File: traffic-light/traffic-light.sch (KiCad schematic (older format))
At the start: 23 parts, among them J1 BATTERY, J10 Traffic_Light_4, J11 ICSP, J2 RFID-RC522_1, J3 RFID-RC522_2, J4 RFID-RC522_3, J5 RFID-RC522_4, J6 Ground, J7 Traffic_Light_1, J8 Traffic_Light_2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

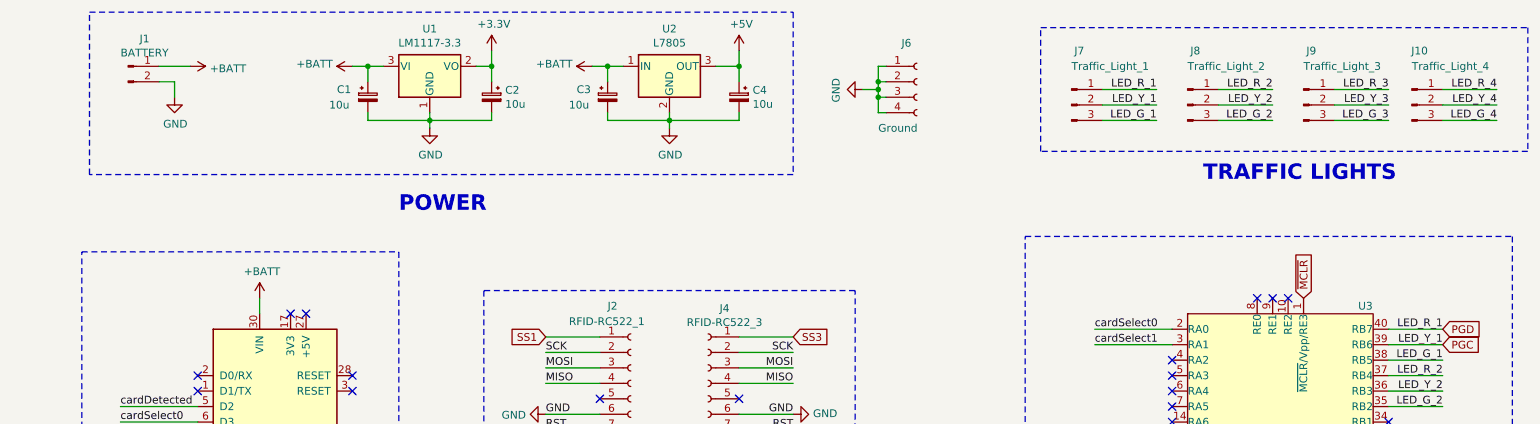
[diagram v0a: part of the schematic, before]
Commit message: Added diode and switch.
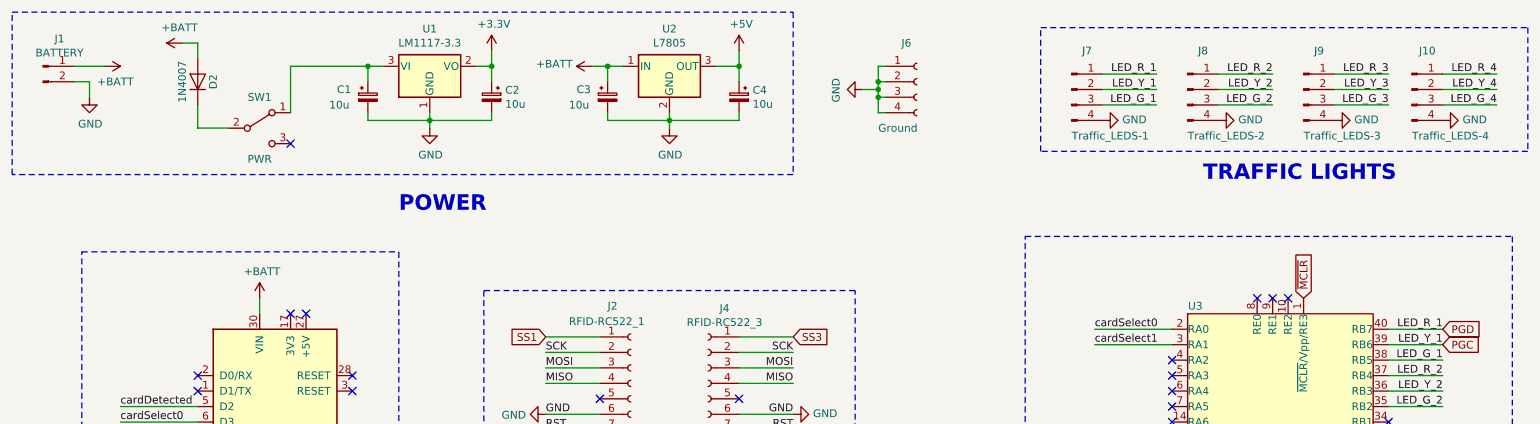
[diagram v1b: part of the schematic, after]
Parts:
- removed J10: Traffic_Light_4, Connector_PinHeader_2.54mm:PinHeader_1x03_P2.54mm_Vertical, symbol Connector:Conn_01x03_Male
- removed J7: Traffic_Light_1, Connector_PinHeader_2.54mm:PinHeader_1x03_P2.54mm_Vertical, symbol Connector:Conn_01x03_Male
- removed J8: Traffic_Light_2, Connector_PinHeader_2.54mm:PinHeader_1x03_P2.54mm_Vertical, symbol Connector:Conn_01x03_Male
- removed J9: Traffic_Light_3, Connector_PinHeader_2.54mm:PinHeader_1x03_P2.54mm_Vertical, symbol Connector:Conn_01x03_Male
- added D2: 1N4007, Diode_THT:D_DO-41_SOD81_P10.16mm_Horizontal, symbol Diode:1N4007
- added J10: Traffic_LEDS-4, Connector_PinHeader_2.54mm:PinHeader_1x04_P2.54mm_Vertical, symbol Connector:Conn_01x04_Male
- added J7: Traffic_LEDS-1, Connector_PinHeader_2.54mm:PinHeader_1x04_P2.54mm_Vertical, symbol Connector:Conn_01x04_Male
- added J8: Traffic_LEDS-2, Connector_PinHeader_2.54mm:PinHeader_1x04_P2.54mm_Vertical, symbol Connector:Conn_01x04_Male
- added J9: Traffic_LEDS-3, Connector_PinHeader_2.54mm:PinHeader_1x04_P2.54mm_Vertical, symbol Connector:Conn_01x04_Male
- added SW1: PWR, Connector_PinSocket_2.54mm:PinSocket_1x03_P2.54mm_Vertical, symbol Switch:SW_SPDT
- J6: footprint Connector_PinHeader_2.54mm:PinHeader_1x04_P2.54mm_Horizontal -> Connector_PinHeader_2.54mm:PinHeader_1x04_P2.54mm_Vertical
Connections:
- net +BATT: now also D2.2 (A); no longer C1.1, U1.3 (VI)
- net GND: now also J10.4 (Pin_4), J7.4 (Pin_4), J8.4 (Pin_4), J9.4 (Pin_4)
- net LED_G_1: now also J7.3 (Pin_3)
- net LED_G_2: now also J8.3 (Pin_3)
- net LED_G_3: now also J9.3 (Pin_3)
- net LED_G_4: now also J10.3 (Pin_3)
- net LED_R_2: now also J8.1 (Pin_1)
- net LED_R_3: now also J9.1 (Pin_1)
- net LED_R_4: now also J10.1 (Pin_1)
- net LED_Y_2: now also J8.2 (Pin_2)
- net LED_Y_3: now also J9.2 (Pin_2)
- net LED_Y_4: now also J10.2 (Pin_2)
- net PGC: now also J7.2 (Pin_2)
- net PGD: now also J7.1 (Pin_1)
- new net: C1.1, SW1.1 (A), U1.3 (VI)
- new net: D2.1 (K), SW1.2 (B)
- no-connect marks 40 -> 41
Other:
- moved on the sheet: J1
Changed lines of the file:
@@
 L Connector:Conn_01x02_Male J1
 U 1 1 5BF6B5A2
-P 1400 1700
-F 0 "J1" H 1506 1878 50  0000 C CNN
-F 1 "BATTERY" H 1506 1787 50  0000 C CNN
-F 2 "Connector_PinHeader_2.54mm:PinHeader_1x02_P2.54mm_Vertical" H 1400 1700 50  0001 C CNN
-F 3 "~" H 1400 1700 50  0001 C CNN
-	1    1400 1700
+P 850 1700
+F 0 "J1" H 956 1878 50  0000 C CNN
+F 1 "BATTERY" H 956 1787 50  0000 C CNN
+F 2 "Connector_PinHeader_2.54mm:PinHeader_1x02_P2.54mm_Vertical" H 850 1700 50  0001 C CNN
+F 3 "~" H 850 1700 50  0001 C CNN
+	1    850  1700
 	1    0    0    -1
 $EndComp
@@
 L power:GND #PWR01
 U 1 1 5BF6B66D
-P 1700 1900
-F 0 "#PWR01" H 1700 1650 50  0001 C CNN
-F 1 "GND" H 1705 1727 50  0000 C CNN
-F 2 "" H 1700 1900 50  0001 C CNN
-F 3 "" H 1700 1900 50  0001 C CNN
-	1    1700 1900
-	1    0    0    -1
-$EndComp
-Wire Wire Line
-	1700 1900 1700 1800
-Wire Wire Line
-	1700 1800 1600 1800
+P 1150 1900
+F 0 "#PWR01" H 1150 1650 50  0001 C CNN
+F 1 "GND" H 1155 1727 50  0000 C CNN
+F 2 "" H 1150 1900 50  0001 C CNN
+F 3 "" H 1150 1900 50  0001 C CNN
+	1    1150 1900
+	1    0    0    -1
+$EndComp
+Wire Wire Line
+	1150 1900 1150 1800
+Wire Wire Line
+	1150 1800 1050 1800
 $Comp
 L power:+BATT #PWR02
 U 1 1 5BF6B6AF
-P 1800 1700
-F 0 "#PWR02" H 1800 1550 50  0001 C CNN
-F 1 "+BATT" V 1815 1828 50  0000 L CNN
-F 2 "" H 1800 1700 50  0001 C CNN
-F 3 "" H 1800 1700 50  0001 C CNN
-	1    1800 1700
+P 1250 1700
+F 0 "#PWR02" H 1250 1550 50  0001 C CNN
+F 1 "+BATT" V 1350 1650 50  0000 L CNN
+F 2 "" H 1250 1700 50  0001 C CNN
+F 3 "" H 1250 1700 50  0001 C CNN
+	1    1250 1700
 	0    1    1    0
 $EndComp
 Wire Wire Line
-	1800 1700 1600 1700
+	1250 1700 1050 1700
 $Comp
 L power:+3.3V #PWR08
@@
 L power:+BATT #PWR06
 U 1 1 5BF6B861
-P 2850 1700
-F 0 "#PWR06" H 2850 1550 50  0001 C CNN
-F 1 "+BATT" V 2865 1827 50  0000 L CNN
-F 2 "" H 2850 1700 50  0001 C CNN
-F 3 "" H 2850 1700 50  0001 C CNN
-	1    2850 1700
-	0    -1   -1   0
-$EndComp
-Wire Wire Line
-	2850 1700 2950 1700
+P 1750 1550
+F 0 "#PWR06" H 1750 1400 50  0001 C CNN
+F 1 "+BATT" V 1850 1450 50  0000 L CNN
+F 2 "" H 1750 1550 50  0001 C CNN
+F 3 "" H 1750 1550 50  0001 C CNN
+	1    1750 1550
+	0    -1   -1   0
+$EndComp
 $Comp
 L power:+BATT #PWR013
@@
 $EndComp
 Wire Notes Line
-	1150 1350 5700 1350
+	650  1350 5700 1350
 Wire Notes Line
 	5700 1350 5700 2400
 Wire Notes Line
-	5700 2400 1150 2400
-Wire Notes Line
-	1150 2400 1150 1350
+	5700 2400 650  2400
+Wire Notes Line
+	650  2400 650  1350
 Text Notes 3150 2650 0    100  ~ 20
 POWER
@@
 Text Label 1550 4700 0    50   ~ 0
 LED
-$Comp
-L Connector:Conn_01x03_Male J7
-U 1 1 5BFC7224
-P 7500 1950
-F 0 "J7" H 7550 2300 50  0000 C CNN
-F 1 "Traffic_Light_1" H 7750 2200 50  0000 C CNN
-F 2 "Connector_PinHeader_2.54mm:PinHeader_1x03_P2.54mm_Vertical" H 7500 1950 50  0001 C CNN
-F 3 "~" H 7500 1950 50  0001 C CNN
-	1    7500 1950
-	1    0    0    -1
-$EndComp
 Wire Wire Line
 	9550 3400 9900 3400
@@
 Text Label 9900 3600 2    50   ~ 0
 LED_G_1
-$Comp
-L Connector:Conn_01x03_Male J8
-U 1 1 5BFD5971
-P 8250 1950
-F 0 "J8" H 8300 2300 50  0000 C CNN
-F 1 "Traffic_Light_2" H 8500 2200 50  0000 C CNN
-F 2 "Connector_PinHeader_2.54mm:PinHeader_1x03_P2.54mm_Vertical" H 8250 1950 50  0001 C CNN
-F 3 "~" H 8250 1950 50  0001 C CNN
-	1    8250 1950
-	1    0    0    -1
-$EndComp
 Wire Wire Line
 	9550 3700 9900 3700
@@
 Text Label 9900 3900 2    50   ~ 0
 LED_G_2
-$Comp
-L Connector:Conn_01x03_Male J9
-U 1 1 5BFD8252
-P 9000 1950
-F 0 "J9" H 9050 2300 50  0000 C CNN
-F 1 "Traffic_Light_3" H 9250 2200 50  0000 C CNN
-F 2 "Connector_PinHeader_2.54mm:PinHeader_1x03_P2.54mm_Vertical" H 9000 1950 50  0001 C CNN
-F 3 "~" H 9000 1950 50  0001 C CNN
-	1    9000 1950
-	1    0    0    -1
-$EndComp
+Wire Wire Line
+	9200 1750 9550 1750
 Wire Wire Line
 	9200 1850 9550 1850
 Wire Wire Line
 	9200 1950 9550 1950
-Wire Wire Line
-	9200 2050 9550 2050
+Text Label 9550 1750 2    50   ~ 0
+LED_R_3
 Text Label 9550 1850 2    50   ~ 0
-LED_R_3
+LED_Y_3
 Text Label 9550 1950 2    50   ~ 0
-LED_Y_3
-Text Label 9550 2050 2    50   ~ 0
 LED_G_3
-$Comp
-L Connector:Conn_01x03_Male J10
-U 1 1 5BFDADCC
-P 9700 1950
-F 0 "J10" H 9750 2300 50  0000 C CNN
-F 1 "Traffic_Light_4" H 9950 2200 50  0000 C CNN
-F 2 "Connector_PinHeader_2.54mm:PinHeader_1x03_P2.54mm_Vertical" H 9700 1950 50  0001 C CNN
-F 3 "~" H 9700 1950 50  0001 C CNN
-	1    9700 1950
-	1    0    0    -1
-$EndComp
+Wire Wire Line
+	9900 1750 10250 1750
 Wire Wire Line
 	9900 1850 10250 1850
 Wire Wire Line
 	9900 1950 10250 1950
-Wire Wire Line
-	9900 2050 10250 2050
+Text Label 10250 1750 2    50   ~ 0
+LED_R_4
 Text Label 10250 1850 2    50   ~ 0
-LED_R_4
+LED_Y_4
 Text Label 10250 1950 2    50   ~ 0
-LED_Y_4
-Text Label 10250 2050 2    50   ~ 0
 LED_G_4
 NoConn ~ 5350 3850
@@
 NoConn ~ 4450 3850
 $Comp
-L Traffic_Light:PIC18F45K22 U3
-U 1 1 5C054184
-P 8850 4200
-F 0 "U3" H 9400 5150 50  0000 C CNN
-F 1 "PIC18F45K22" H 8850 4200 50  0000 C CNN
-F 2 "Package_DIP:DIP-40_W15.24mm_LongPads" V 8850 5100 50  0001 C CNN
-F 3 "https://www.microchip.com/stellent/groups/picmicro_sg/documents/devicedoc/cn547043.pdf" V 8850 5100 50  0001 C CNN
-	1    8850 4200
-	1    0    0    -1
-$EndComp
-$Comp
 L power:+5V #PWR0101
 U 1 1 5C058212
@@
 	8950 5300 8950 5200
 Wire Wire Line
+	7700 1750 8050 1750
+Wire Wire Line
 	7700 1850 8050 1850
 Wire Wire Line
 	7700 1950 8050 1950
-Wire Wire Line
-	7700 2050 8050 2050
+Text Label 8050 1750 2    50   ~ 0
+LED_R_1
 Text Label 8050 1850 2    50   ~ 0
-LED_R_1
+LED_Y_1
 Text Label 8050 1950 2    50   ~ 0
-LED_Y_1
-Text Label 8050 2050 2    50   ~ 0
 LED_G_1
 Wire Wire Line
+	8450 1750 8800 1750
+Wire Wire Line
 	8450 1850 8800 1850
 Wire Wire Line
 	8450 1950 8800 1950
-Wire Wire Line
-	8450 2050 8800 2050
+Text Label 8800 1750 2    50   ~ 0
+LED_R_2
 Text Label 8800 1850 2    50   ~ 0
-LED_R_2
+LED_Y_2
 Text Label 8800 1950 2    50   ~ 0
-LED_Y_2
-Text Label 8800 2050 2    50   ~ 0
 LED_G_2
 Wire Wire Line
@@
 F 0 "J6" H 6400 2050 50  0000 L CNN
 F 1 "Ground" H 6250 1500 50  0000 L CNN
-F 2 "Connector_PinHeader_2.54mm:PinHeader_1x04_P2.54mm_Horizontal" H 6500 1800 50  0001 C CNN
+F 2 "Connector_PinHeader_2.54mm:PinHeader_1x04_P2.54mm_Vertical" H 6500 1800 50  0001 C CNN
 F 3 "~" H 6500 1800 50  0001 C CNN
 	1    6500 1800
@@
 Wire Wire Line
 	6250 1850 6250 1900
+$Comp
+L Diode:1N4007 D2
+U 1 1 5C6B1FD6
+P 1850 1800
+F 0 "D2" H 1850 1700 50  0000 C CNN
+F 1 "1N4007" H 1850 1900 50  0000 C CNN
+F 2 "Diode_THT:D_DO-41_SOD81_P10.16mm_Horizontal" H 1850 1625 50  0001 C CNN
+F 3 "http://www.vishay.com/docs/88503/1n4001.pdf" H 1850 1800 50  0001 C CNN
+	1    1850 1800
+	0    -1   -1   0
+$EndComp
+$Comp
+L Switch:SW_SPDT SW1
+U 1 1 5C6B219A
+P 2250 2100
+F 0 "SW1" H 2250 2300 50  0000 C CNN
+F 1 "PWR" H 2250 1900 50  0000 C CNN
+F 2 "Connector_PinSocket_2.54mm:PinSocket_1x03_P2.54mm_Vertical" H 2250 2100 50  0001 C CNN
+F 3 "" H 2250 2100 50  0001 C CNN
+	1    2250 2100
+	1    0    0    -1
+$EndComp
+Wire Wire Line
+	2450 1700 2450 2000
+Wire Wire Line
+	2450 1700 2950 1700
+Wire Wire Line
+	1850 1950 1850 2100
+Wire Wire Line
+	1850 2100 2050 2100
+Wire Wire Line
+	1850 1650 1850 1550
+Wire Wire Line
+	1850 1550 1750 1550
+NoConn ~ 2450 2200
+$Comp
+L Connector:Conn_01x04_Male J7
+U 1 1 5C6D68B3
+P 7500 1850
+F 0 "J7" H 7600 2100 50  0000 C CNN
+F 1 "Traffic_LEDS-1" H 7750 1550 50  0000 C CNN
+F 2 "Connector_PinHeader_2.54mm:PinHeader_1x04_P2.54mm_Vertical" H 7500 1850 50  0001 C CNN
+F 3 "~" H 7500 1850 50  0001 C CNN
+	1    7500 1850
+	1    0    0    -1
+$EndComp
+$Comp
+L power:GND #PWR0105
+U 1 1 5C6DCD0F
+P 7700 2050
+F 0 "#PWR0105" H 7700 1800 50  0001 C CNN
+F 1 "GND" V 7705 1922 50  0000 R CNN
+F 2 "" H 7700 2050 50  0001 C CNN
+F 3 "" H 7700 2050 50  0001 C CNN
+	1    7700 2050
+	0    -1   -1   0
+$EndComp
+$Comp
+L Connector:Conn_01x04_Male J8
+U 1 1 5C6DCDDB
+P 8250 1850
+F 0 "J8" H 8350 2100 50  0000 C CNN
+F 1 "Traffic_LEDS-2" H 8500 1550 50  0000 C CNN
+F 2 "Connector_PinHeader_2.54mm:PinHeader_1x04_P2.54mm_Vertical" H 8250 1850 50  0001 C CNN
+F 3 "~" H 8250 1850 50  0001 C CNN
+	1    8250 1850
+	1    0    0    -1
+$EndComp
+$Comp
+L Connector:Conn_01x04_Male J9
+U 1 1 5C6DCE39
+P 9000 1850
+F 0 "J9" H 9100 2100 50  0000 C CNN
+F 1 "Traffic_LEDS-3" H 9250 1550 50  0000 C CNN
+F 2 "Connector_PinHeader_2.54mm:PinHeader_1x04_P2.54mm_Vertical" H 9000 1850 50  0001 C CNN
+F 3 "~" H 9000 1850 50  0001 C CNN
+	1    9000 1850
+	1    0    0    -1
+$EndComp
+$Comp
+L Connector:Conn_01x04_Male J10
+U 1 1 5C6DCE95
+P 9700 1850
+F 0 "J10" H 9800 2100 50  0000 C CNN
+F 1 "Traffic_LEDS-4" H 9950 1550 50  0000 C CNN
+F 2 "Connector_PinHeader_2.54mm:PinHeader_1x04_P2.54mm_Vertical" H 9700 1850 50  0001 C CNN
+F 3 "~" H 9700 1850 50  0001 C CNN
+	1    9700 1850
+	1    0    0    -1
+$EndComp
+$Comp
+L power:GND #PWR0106
+U 1 1 5C6DCFE5
+P 8450 2050
+F 0 "#PWR0106" H 8450 1800 50  0001 C CNN
+F 1 "GND" V 8455 1922 50  0000 R CNN
+F 2 "" H 8450 2050 50  0001 C CNN
+F 3 "" H 8450 2050 50  0001 C CNN
+	1    8450 2050
+	0    -1   -1   0
+$EndComp
+$Comp
+L power:GND #PWR0107
+U 1 1 5C6DD022
+P 9200 2050
+F 0 "#PWR0107" H 9200 1800 50  0001 C CNN
+F 1 "GND" V 9205 1922 50  0000 R CNN
+F 2 "" H 9200 2050 50  0001 C CNN
+F 3 "" H 9200 2050 50  0001 C CNN
+	1    9200 2050
+	0    -1   -1   0
+$EndComp
+$Comp
+L power:GND #PWR0108
+U 1 1 5C6DD05F
+P 9900 2050
+F 0 "#PWR0108" H 9900 1800 50  0001 C CNN
+F 1 "GND" V 9905 1922 50  0000 R CNN
+F 2 "" H 9900 2050 50  0001 C CNN
+F 3 "" H 9900 2050 50  0001 C CNN
+	1    9900 2050
+	0    -1   -1   0
+$EndComp
+$Comp
+L Traffic_Light:PIC18F45K22 U3
+U 1 1 5C6DD591
+P 8850 4200
+F 0 "U3" H 8300 5150 50  0000 C CNN
+F 1 "PIC18F45K22" H 8850 4200 50  0000 C CNN
+F 2 "Package_DIP:DIP-40_W15.24mm_LongPads" V 8850 5100 50  0001 C CNN
+F 3 "https://www.microchip.com/stellent/groups/picmicro_sg/documents/devicedoc/cn547043.pdf" V 8850 5100 50  0001 C CNN
+	1    8850 4200
+	1    0    0    -1
+$EndComp
 $EndSCHEMATC

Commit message: PCB corrections.
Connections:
- net +BATT: now also D2.1 (K), SW1.2 (B); no longer D2.2 (A), J1.1 (Pin_1)
- new net: D2.2 (A), J1.1 (Pin_1)
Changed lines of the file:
@@
 L power:+BATT #PWR02
 U 1 1 5BF6B6AF
-P 1250 1700
-F 0 "#PWR02" H 1250 1550 50  0001 C CNN
-F 1 "+BATT" V 1350 1650 50  0000 L CNN
-F 2 "" H 1250 1700 50  0001 C CNN
-F 3 "" H 1250 1700 50  0001 C CNN
-	1    1250 1700
-	0    1    1    0
+P 1850 2100
+F 0 "#PWR02" H 1850 1950 50  0001 C CNN
+F 1 "+BATT" V 1950 2050 50  0000 L CNN
+F 2 "" H 1850 2100 50  0001 C CNN
+F 3 "" H 1850 2100 50  0001 C CNN
+	1    1850 2100
+	-1   0    0    1
 $EndComp
 Wire Wire Line
@@
 Wire Wire Line
 	5350 1700 5200 1700
-$Comp
-L power:+BATT #PWR06
-U 1 1 5BF6B861
-P 1750 1550
-F 0 "#PWR06" H 1750 1400 50  0001 C CNN
-F 1 "+BATT" V 1850 1450 50  0000 L CNN
-F 2 "" H 1750 1550 50  0001 C CNN
-F 3 "" H 1750 1550 50  0001 C CNN
-	1    1750 1550
-	0    -1   -1   0
-$EndComp
 $Comp
 L power:+BATT #PWR013
@@
 Wire Wire Line
 	1850 1650 1850 1550
-Wire Wire Line
-	1850 1550 1750 1550
 NoConn ~ 2450 2200
 $Comp
@@
 	1    0    0    -1
 $EndComp
+Connection ~ 1850 2100
+Wire Wire Line
+	1250 1550 1250 1700
+Wire Wire Line
+	1250 1550 1850 1550
 $EndSCHEMATC
